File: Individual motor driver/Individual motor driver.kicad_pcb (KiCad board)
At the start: 2 copper layers, 92.7 x 95.2 mm, 35 parts, among them P1 CONN_01X02, P2 CONN_01X02, P3 CONN_01X02, P4 CONN_01X02, P5 CONN_01X02, P6 CONN_01X02, P7 CONN_01X04, P8 CONN_01X02, Q1 PN2222A, Q2 PN2222A, Q3 PN2222A, Q4 PN2222A, U1 BluePill_STM32F103C, U2 BluePill_STM32F103C, U3 ACS711xLCTR-12AB, U4 ACS711xLCTR-12AB

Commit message: Update files
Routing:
- net Stall_2: track 0.00 -> 97.5 mm, vias 0 -> 1
- net GND: track 33.0 -> 43.4 mm, vias 0 -> 73
- net 3.3v: track 225.4 -> 221.5 mm, vias 7 -> 6
- net (no net): vias 2 -> 0
- added copper zone on B.Cu, net GND
- added copper zone on F.Cu, net GND

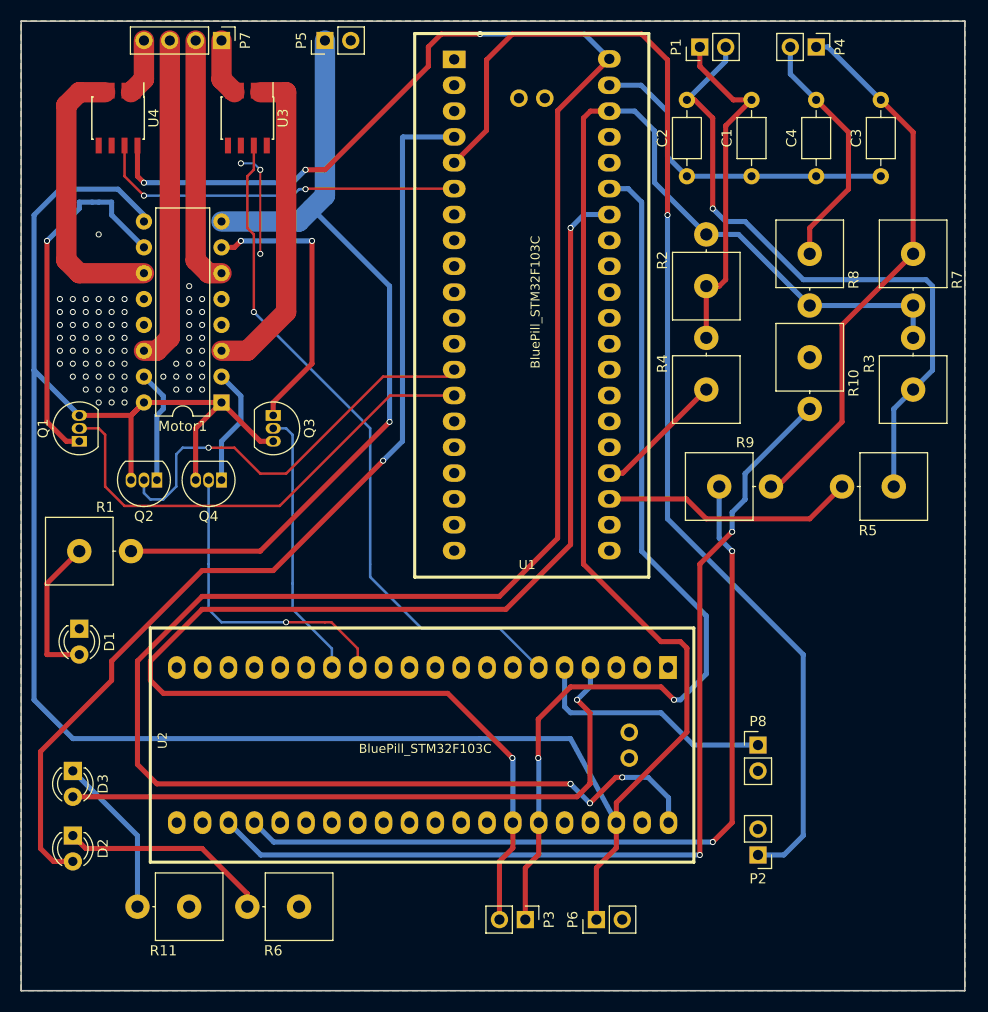
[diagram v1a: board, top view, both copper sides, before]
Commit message: Finished routing and improved some design flaws
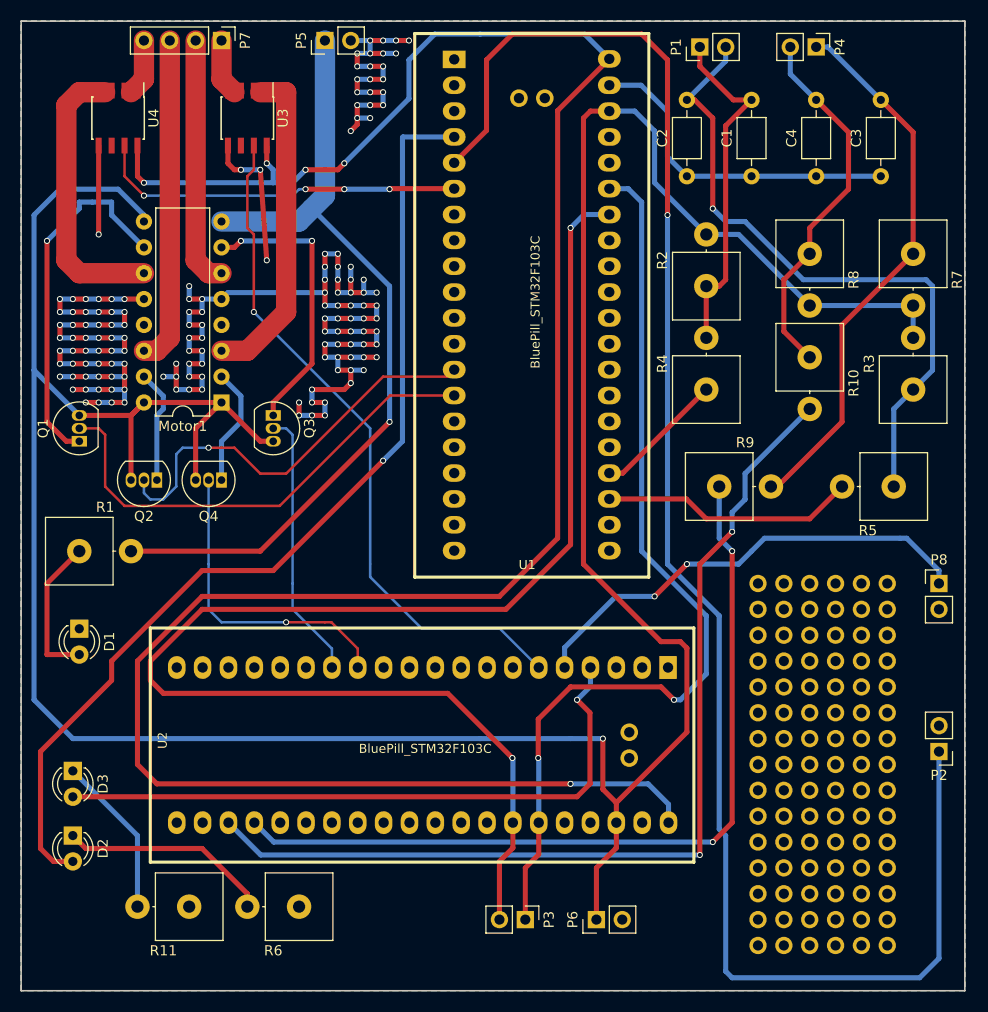
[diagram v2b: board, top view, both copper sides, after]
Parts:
- added REF**: Pin_Header_Straight_1x01_Pitch2.54mm, Pin_Headers:Pin_Header_Straight_1x01_Pitch2.54mm, F.Cu at (130.2, 149.9)
- added REF**: Pin_Header_Straight_1x01_Pitch2.54mm, Pin_Headers:Pin_Header_Straight_1x01_Pitch2.54mm, F.Cu at (122.6, 147.3)
- added REF**: Pin_Header_Straight_1x01_Pitch2.54mm, Pin_Headers:Pin_Header_Straight_1x01_Pitch2.54mm, F.Cu at (120.0, 147.3)
- added REF**: Pin_Header_Straight_1x01_Pitch2.54mm, Pin_Headers:Pin_Header_Straight_1x01_Pitch2.54mm, F.Cu at (117.5, 147.3)
- added REF**: Pin_Header_Straight_1x01_Pitch2.54mm, Pin_Headers:Pin_Header_Straight_1x01_Pitch2.54mm, F.Cu at (130.2, 144.8)
- added REF**: Pin_Header_Straight_1x01_Pitch2.54mm, Pin_Headers:Pin_Header_Straight_1x01_Pitch2.54mm, F.Cu at (127.6, 144.8)
- added REF**: Pin_Header_Straight_1x01_Pitch2.54mm, Pin_Headers:Pin_Header_Straight_1x01_Pitch2.54mm, F.Cu at (125.1, 144.8)
- added REF**: Pin_Header_Straight_1x01_Pitch2.54mm, Pin_Headers:Pin_Header_Straight_1x01_Pitch2.54mm, F.Cu at (122.6, 144.8)
- added REF**: Pin_Header_Straight_1x01_Pitch2.54mm, Pin_Headers:Pin_Header_Straight_1x01_Pitch2.54mm, F.Cu at (120.0, 144.8)
- added REF**: Pin_Header_Straight_1x01_Pitch2.54mm, Pin_Headers:Pin_Header_Straight_1x01_Pitch2.54mm, F.Cu at (117.5, 144.8)
- added REF**: Pin_Header_Straight_1x01_Pitch2.54mm, Pin_Headers:Pin_Header_Straight_1x01_Pitch2.54mm, F.Cu at (130.2, 142.2)
- added REF**: Pin_Header_Straight_1x01_Pitch2.54mm, Pin_Headers:Pin_Header_Straight_1x01_Pitch2.54mm, F.Cu at (127.6, 149.9)
- added REF**: Pin_Header_Straight_1x01_Pitch2.54mm, Pin_Headers:Pin_Header_Straight_1x01_Pitch2.54mm, F.Cu at (127.6, 142.2)
- added REF**: Pin_Header_Straight_1x01_Pitch2.54mm, Pin_Headers:Pin_Header_Straight_1x01_Pitch2.54mm, F.Cu at (125.1, 142.2)
- added REF**: Pin_Header_Straight_1x01_Pitch2.54mm, Pin_Headers:Pin_Header_Straight_1x01_Pitch2.54mm, F.Cu at (122.6, 142.2)
- added REF**: Pin_Header_Straight_1x01_Pitch2.54mm, Pin_Headers:Pin_Header_Straight_1x01_Pitch2.54mm, F.Cu at (120.0, 142.2)
- added REF**: Pin_Header_Straight_1x01_Pitch2.54mm, Pin_Headers:Pin_Header_Straight_1x01_Pitch2.54mm, F.Cu at (117.5, 142.2)
- added REF**: Pin_Header_Straight_1x01_Pitch2.54mm, Pin_Headers:Pin_Header_Straight_1x01_Pitch2.54mm, F.Cu at (130.2, 139.7)
- added REF**: Pin_Header_Straight_1x01_Pitch2.54mm, Pin_Headers:Pin_Header_Straight_1x01_Pitch2.54mm, F.Cu at (127.6, 139.7)
- added REF**: Pin_Header_Straight_1x01_Pitch2.54mm, Pin_Headers:Pin_Header_Straight_1x01_Pitch2.54mm, F.Cu at (125.1, 139.7)
- added REF**: Pin_Header_Straight_1x01_Pitch2.54mm, Pin_Headers:Pin_Header_Straight_1x01_Pitch2.54mm, F.Cu at (122.6, 139.7)
- added REF**: Pin_Header_Straight_1x01_Pitch2.54mm, Pin_Headers:Pin_Header_Straight_1x01_Pitch2.54mm, F.Cu at (120.0, 139.7)
- added REF**: Pin_Header_Straight_1x01_Pitch2.54mm, Pin_Headers:Pin_Header_Straight_1x01_Pitch2.54mm, F.Cu at (125.1, 149.9)
- added REF**: Pin_Header_Straight_1x01_Pitch2.54mm, Pin_Headers:Pin_Header_Straight_1x01_Pitch2.54mm, F.Cu at (117.5, 139.7)
- added REF**: Pin_Header_Straight_1x01_Pitch2.54mm, Pin_Headers:Pin_Header_Straight_1x01_Pitch2.54mm, F.Cu at (130.2, 137.2)
- added REF**: Pin_Header_Straight_1x01_Pitch2.54mm, Pin_Headers:Pin_Header_Straight_1x01_Pitch2.54mm, F.Cu at (127.6, 137.2)
- added REF**: Pin_Header_Straight_1x01_Pitch2.54mm, Pin_Headers:Pin_Header_Straight_1x01_Pitch2.54mm, F.Cu at (125.1, 137.2)
- added REF**: Pin_Header_Straight_1x01_Pitch2.54mm, Pin_Headers:Pin_Header_Straight_1x01_Pitch2.54mm, F.Cu at (122.6, 137.2)
- added REF**: Pin_Header_Straight_1x01_Pitch2.54mm, Pin_Headers:Pin_Header_Straight_1x01_Pitch2.54mm, F.Cu at (120.0, 137.2)
- added REF**: Pin_Header_Straight_1x01_Pitch2.54mm, Pin_Headers:Pin_Header_Straight_1x01_Pitch2.54mm, F.Cu at (117.5, 137.2)
- added REF**: Pin_Header_Straight_1x01_Pitch2.54mm, Pin_Headers:Pin_Header_Straight_1x01_Pitch2.54mm, F.Cu at (130.2, 134.6)
- added REF**: Pin_Header_Straight_1x01_Pitch2.54mm, Pin_Headers:Pin_Header_Straight_1x01_Pitch2.54mm, F.Cu at (127.6, 134.6)
- added REF**: Pin_Header_Straight_1x01_Pitch2.54mm, Pin_Headers:Pin_Header_Straight_1x01_Pitch2.54mm, F.Cu at (125.1, 134.6)
- added REF**: Pin_Header_Straight_1x01_Pitch2.54mm, Pin_Headers:Pin_Header_Straight_1x01_Pitch2.54mm, F.Cu at (122.6, 149.9)
- added REF**: Pin_Header_Straight_1x01_Pitch2.54mm, Pin_Headers:Pin_Header_Straight_1x01_Pitch2.54mm, F.Cu at (122.6, 134.6)
- added REF**: Pin_Header_Straight_1x01_Pitch2.54mm, Pin_Headers:Pin_Header_Straight_1x01_Pitch2.54mm, F.Cu at (120.0, 134.6)
- added REF**: Pin_Header_Straight_1x01_Pitch2.54mm, Pin_Headers:Pin_Header_Straight_1x01_Pitch2.54mm, F.Cu at (117.5, 134.6)
- added REF**: Pin_Header_Straight_1x01_Pitch2.54mm, Pin_Headers:Pin_Header_Straight_1x01_Pitch2.54mm, F.Cu at (130.2, 132.1)
- added REF**: Pin_Header_Straight_1x01_Pitch2.54mm, Pin_Headers:Pin_Header_Straight_1x01_Pitch2.54mm, F.Cu at (127.6, 132.1)
- added REF**: Pin_Header_Straight_1x01_Pitch2.54mm, Pin_Headers:Pin_Header_Straight_1x01_Pitch2.54mm, F.Cu at (125.1, 132.1)
- added REF**: Pin_Header_Straight_1x01_Pitch2.54mm, Pin_Headers:Pin_Header_Straight_1x01_Pitch2.54mm, F.Cu at (122.6, 132.1)
- added REF**: Pin_Header_Straight_1x01_Pitch2.54mm, Pin_Headers:Pin_Header_Straight_1x01_Pitch2.54mm, F.Cu at (120.0, 132.1)
- added REF**: Pin_Header_Straight_1x01_Pitch2.54mm, Pin_Headers:Pin_Header_Straight_1x01_Pitch2.54mm, F.Cu at (117.5, 132.1)
- added REF**: Pin_Header_Straight_1x01_Pitch2.54mm, Pin_Headers:Pin_Header_Straight_1x01_Pitch2.54mm, F.Cu at (130.2, 129.5)
- added REF**: Pin_Header_Straight_1x01_Pitch2.54mm, Pin_Headers:Pin_Header_Straight_1x01_Pitch2.54mm, F.Cu at (120.0, 149.9)
- added REF**: Pin_Header_Straight_1x01_Pitch2.54mm, Pin_Headers:Pin_Header_Straight_1x01_Pitch2.54mm, F.Cu at (127.6, 129.5)
- added REF**: Pin_Header_Straight_1x01_Pitch2.54mm, Pin_Headers:Pin_Header_Straight_1x01_Pitch2.54mm, F.Cu at (125.1, 129.5)
- added REF**: Pin_Header_Straight_1x01_Pitch2.54mm, Pin_Headers:Pin_Header_Straight_1x01_Pitch2.54mm, F.Cu at (122.6, 129.5)
- added REF**: Pin_Header_Straight_1x01_Pitch2.54mm, Pin_Headers:Pin_Header_Straight_1x01_Pitch2.54mm, F.Cu at (120.0, 129.5)
- added REF**: Pin_Header_Straight_1x01_Pitch2.54mm, Pin_Headers:Pin_Header_Straight_1x01_Pitch2.54mm, F.Cu at (117.5, 129.5)
- added REF**: Pin_Header_Straight_1x01_Pitch2.54mm, Pin_Headers:Pin_Header_Straight_1x01_Pitch2.54mm, F.Cu at (130.2, 127.0)
- added REF**: Pin_Header_Straight_1x01_Pitch2.54mm, Pin_Headers:Pin_Header_Straight_1x01_Pitch2.54mm, F.Cu at (127.6, 127.0)
- added REF**: Pin_Header_Straight_1x01_Pitch2.54mm, Pin_Headers:Pin_Header_Straight_1x01_Pitch2.54mm, F.Cu at (125.1, 127.0)
- added REF**: Pin_Header_Straight_1x01_Pitch2.54mm, Pin_Headers:Pin_Header_Straight_1x01_Pitch2.54mm, F.Cu at (122.6, 127.0)
- added REF**: Pin_Header_Straight_1x01_Pitch2.54mm, Pin_Headers:Pin_Header_Straight_1x01_Pitch2.54mm, F.Cu at (120.0, 127.0)
- added REF**: Pin_Header_Straight_1x01_Pitch2.54mm, Pin_Headers:Pin_Header_Straight_1x01_Pitch2.54mm, F.Cu at (117.5, 149.9)
- added REF**: Pin_Header_Straight_1x01_Pitch2.54mm, Pin_Headers:Pin_Header_Straight_1x01_Pitch2.54mm, F.Cu at (117.5, 127.0)
- added REF**: Pin_Header_Straight_1x01_Pitch2.54mm, Pin_Headers:Pin_Header_Straight_1x01_Pitch2.54mm, F.Cu at (130.2, 124.5)
- added REF**: Pin_Header_Straight_1x01_Pitch2.54mm, Pin_Headers:Pin_Header_Straight_1x01_Pitch2.54mm, F.Cu at (127.6, 124.5)
- added REF**: Pin_Header_Straight_1x01_Pitch2.54mm, Pin_Headers:Pin_Header_Straight_1x01_Pitch2.54mm, F.Cu at (125.1, 124.5)
- added REF**: Pin_Header_Straight_1x01_Pitch2.54mm, Pin_Headers:Pin_Header_Straight_1x01_Pitch2.54mm, F.Cu at (122.6, 124.5)
- added REF**: Pin_Header_Straight_1x01_Pitch2.54mm, Pin_Headers:Pin_Header_Straight_1x01_Pitch2.54mm, F.Cu at (120.0, 124.5)
- added REF**: Pin_Header_Straight_1x01_Pitch2.54mm, Pin_Headers:Pin_Header_Straight_1x01_Pitch2.54mm, F.Cu at (117.5, 124.5)
- added REF**: Pin_Header_Straight_1x01_Pitch2.54mm, Pin_Headers:Pin_Header_Straight_1x01_Pitch2.54mm, F.Cu at (130.2, 121.9)
- added REF**: Pin_Header_Straight_1x01_Pitch2.54mm, Pin_Headers:Pin_Header_Straight_1x01_Pitch2.54mm, F.Cu at (127.6, 121.9)
- added REF**: Pin_Header_Straight_1x01_Pitch2.54mm, Pin_Headers:Pin_Header_Straight_1x01_Pitch2.54mm, F.Cu at (125.1, 121.9)
- added REF**: Pin_Header_Straight_1x01_Pitch2.54mm, Pin_Headers:Pin_Header_Straight_1x01_Pitch2.54mm, F.Cu at (130.2, 147.3)
- added REF**: Pin_Header_Straight_1x01_Pitch2.54mm, Pin_Headers:Pin_Header_Straight_1x01_Pitch2.54mm, F.Cu at (122.6, 121.9)
- added REF**: Pin_Header_Straight_1x01_Pitch2.54mm, Pin_Headers:Pin_Header_Straight_1x01_Pitch2.54mm, F.Cu at (120.0, 121.9)
- added REF**: Pin_Header_Straight_1x01_Pitch2.54mm, Pin_Headers:Pin_Header_Straight_1x01_Pitch2.54mm, F.Cu at (117.5, 121.9)
- added REF**: Pin_Header_Straight_1x01_Pitch2.54mm, Pin_Headers:Pin_Header_Straight_1x01_Pitch2.54mm, F.Cu at (130.2, 119.4)
- added REF**: Pin_Header_Straight_1x01_Pitch2.54mm, Pin_Headers:Pin_Header_Straight_1x01_Pitch2.54mm, F.Cu at (127.6, 119.4)
- added REF**: Pin_Header_Straight_1x01_Pitch2.54mm, Pin_Headers:Pin_Header_Straight_1x01_Pitch2.54mm, F.Cu at (125.1, 119.4)
- added REF**: Pin_Header_Straight_1x01_Pitch2.54mm, Pin_Headers:Pin_Header_Straight_1x01_Pitch2.54mm, F.Cu at (122.6, 119.4)
- added REF**: Pin_Header_Straight_1x01_Pitch2.54mm, Pin_Headers:Pin_Header_Straight_1x01_Pitch2.54mm, F.Cu at (120.0, 119.4)
- added REF**: Pin_Header_Straight_1x01_Pitch2.54mm, Pin_Headers:Pin_Header_Straight_1x01_Pitch2.54mm, F.Cu at (117.5, 119.4)
- added REF**: Pin_Header_Straight_1x01_Pitch2.54mm, Pin_Headers:Pin_Header_Straight_1x01_Pitch2.54mm, F.Cu at (130.2, 116.8)
- added REF**: Pin_Header_Straight_1x01_Pitch2.54mm, Pin_Headers:Pin_Header_Straight_1x01_Pitch2.54mm, F.Cu at (127.6, 147.3)
- added REF**: Pin_Header_Straight_1x01_Pitch2.54mm, Pin_Headers:Pin_Header_Straight_1x01_Pitch2.54mm, F.Cu at (127.6, 116.8)
- added REF**: Pin_Header_Straight_1x01_Pitch2.54mm, Pin_Headers:Pin_Header_Straight_1x01_Pitch2.54mm, F.Cu at (125.1, 116.8)
- added REF**: Pin_Header_Straight_1x01_Pitch2.54mm, Pin_Headers:Pin_Header_Straight_1x01_Pitch2.54mm, F.Cu at (122.6, 116.8)
- added REF**: Pin_Header_Straight_1x01_Pitch2.54mm, Pin_Headers:Pin_Header_Straight_1x01_Pitch2.54mm, F.Cu at (120.0, 116.8)
- added REF**: Pin_Header_Straight_1x01_Pitch2.54mm, Pin_Headers:Pin_Header_Straight_1x01_Pitch2.54mm, F.Cu at (117.5, 116.8)
- added REF**: Pin_Header_Straight_1x01_Pitch2.54mm, Pin_Headers:Pin_Header_Straight_1x01_Pitch2.54mm, F.Cu at (130.2, 114.3)
- added REF**: Pin_Header_Straight_1x01_Pitch2.54mm, Pin_Headers:Pin_Header_Straight_1x01_Pitch2.54mm, F.Cu at (127.6, 114.3)
- added REF**: Pin_Header_Straight_1x01_Pitch2.54mm, Pin_Headers:Pin_Header_Straight_1x01_Pitch2.54mm, F.Cu at (125.1, 114.3)
- added REF**: Pin_Header_Straight_1x01_Pitch2.54mm, Pin_Headers:Pin_Header_Straight_1x01_Pitch2.54mm, F.Cu at (122.6, 114.3)
- added REF**: Pin_Header_Straight_1x01_Pitch2.54mm, Pin_Headers:Pin_Header_Straight_1x01_Pitch2.54mm, F.Cu at (120.0, 114.3)
- added REF**: Pin_Header_Straight_1x01_Pitch2.54mm, Pin_Headers:Pin_Header_Straight_1x01_Pitch2.54mm, F.Cu at (125.1, 147.3)
- added REF**: Pin_Header_Straight_1x01_Pitch2.54mm, Pin_Headers:Pin_Header_Straight_1x01_Pitch2.54mm, F.Cu at (117.5, 114.3)
- moved P8 23.8 mm to (135.3, 114.3)
- moved P2 20.5 mm to (135.3, 130.8)
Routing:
- net GND: track 43.4 -> 254.1 mm, vias 73 -> 149
- net Limit2: track 118.3 -> 165.5 mm
- net Limit1: track 24.4 -> 45.8 mm, vias 0 -> 2
- net Net-(C4-Pad2): track 24.3 -> 36.5 mm
- net 3.3v: track 221.5 -> 224.1 mm, vias 6 -> 5
- net 5V: track 303.6 -> 304.2 mm, vias 0 -> 1
- net M2:Current: vias 2 -> 4

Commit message: PCB updates
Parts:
- added P9: CONN_01X02, Connector_PinHeader_2.54mm:PinHeader_1x02_P2.54mm_Vertical, F.Cu at (94.6, 151.8)
- added REF**: MountingHole_3.2mm_M3, MountingHole:MountingHole_3.2mm_M3, F.Cu at (48.9, 150.5)
- added REF**: MountingHole_3.2mm_M3, MountingHole:MountingHole_3.2mm_M3, F.Cu at (48.9, 62.9)
- added REF**: MountingHole_3.2mm_M3, MountingHole:MountingHole_3.2mm_M3, F.Cu at (134.0, 62.9)
- added REF**: MountingHole_3.2mm_M3, MountingHole:MountingHole_3.2mm_M3, F.Cu at (110.5, 150.5)
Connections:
- REF** pad 1: (no net) -> GND (x6)
- REF** pad 1: (no net) -> 5V (x6)
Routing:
- net 5V: track 304.2 -> 335.6 mm, vias 1 -> 2
- net SDA: track 92.4 -> 96.8 mm
- net SCL: track 138.5 -> 143.0 mm
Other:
- outline, holes or cut-outs redrawn
- board text added: "5V"
- board text added: "Designed and made by Ethan. Class of 2020 https://github.com/ethanleep/robotic-arm"
- board text added: "GND"
- board text added: "Voltage range: 4.5V - 36V Max current: 1A per motor Overall max current: 2A"

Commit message: Misc. Changes to PCB
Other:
- board text added: "Prototyping Area"
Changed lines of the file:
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@@
     (area 45.009999 58.979999 137.870001 154.380001)
     (thickness 1.6)
-    (drawings 45)
+    (drawings 46)
     (tracks 691)
     (zones 0)
@@
   )
   (setup
-    (last_trace_width 0.5)
+    (last_trace_width 0.25)
     (user_trace_width 0.2)
     (user_trace_width 0.25)
@@
     (pad 1 np_thru_hole circle (at 0 0) (size 3.2 3.2) (drill 3.2) (layers *.Cu *.Mask))
   )
+  (gr_text "Prototyping Area" (at 114.3 128.27 90) (layer F.SilkS)
+    (effects (font (size 1.5 1.5) (thickness 0.3)))
+  )
+  (dimension 95.25 (width 0.3) (layer Cmts.User)
+    (gr_text "95.250 mm" (at 25.955001 106.68 270) (layer Cmts.User)
+      (effects (font (size 1.5 1.5) (thickness 0.3)))
+    )
+    (feature1 (pts (xy 49.53 154.305) (xy 24.605001 154.305)))
+    (feature2 (pts (xy 49.53 59.055) (xy 24.605001 59.055)))
+    (crossbar (pts (xy 27.305001 59.055) (xy 27.305001 154.305)))
+    (arrow1a (pts (xy 27.305001 154.305) (xy 26.71858 153.178496)))
+    (arrow1b (pts (xy 27.305001 154.305) (xy 27.891422 153.178496)))
+    (arrow2a (pts (xy 27.305001 59.055) (xy 26.71858 60.181504)))
+    (arrow2b (pts (xy 27.305001 59.055) (xy 27.891422 60.181504)))
+  )
+  (dimension 92.71 (width 0.3) (layer Cmts.User)
+    (gr_text "92.710 mm" (at 91.44 46.275) (layer Cmts.User)
+      (effects (font (size 1.5 1.5) (thickness 0.3)))
+    )
+    (feature1 (pts (xy 137.795 63.5) (xy 137.795 44.925)))
+    (feature2 (pts (xy 45.085 63.5) (xy 45.085 44.925)))
+    (crossbar (pts (xy 45.085 47.625) (xy 137.795 47.625)))
+    (arrow1a (pts (xy 137.795 47.625) (xy 136.668496 48.211421)))
+    (arrow1b (pts (xy 137.795 47.625) (xy 136.668496 47.038579)))
+    (arrow2a (pts (xy 45.085 47.625) (xy 46.211504 48.211421)))
+    (arrow2b (pts (xy 45.085 47.625) (xy 46.211504 47.038579)))
+  )
   (gr_text "Voltage range: 4.5V - 36V\nMax current: 1A per motor\nOverall max current: 2A" (at 60.96 71.12) (layer B.SilkS)
     (effects (font (size 1.5 1.5) (thickness 0.3)) (justify mirror))
@@
     (effects (font (size 1.5 1.5) (thickness 0.3)))
   )
-  (dimension 87.63 (width 0.3) (layer Cmts.User)
-    (gr_text "87.630 mm" (at 88.9 39.29) (layer Cmts.User)
-      (effects (font (size 1.5 1.5) (thickness 0.3)))
-    )
-    (feature1 (pts (xy 132.715 59.055) (xy 132.715 37.94)))
-    (feature2 (pts (xy 45.085 59.055) (xy 45.085 37.94)))
-    (crossbar (pts (xy 45.085 40.64) (xy 132.715 40.64)))
-    (arrow1a (pts (xy 132.715 40.64) (xy 131.588496 41.226421)))
-    (arrow1b (pts (xy 132.715 40.64) (xy 131.588496 40.053579)))
-    (arrow2a (pts (xy 45.085 40.64) (xy 46.211504 41.226421)))
-    (arrow2b (pts (xy 45.085 40.64) (xy 46.211504 40.053579)))
-  )
-  (dimension 97.155 (width 0.3) (layer Cmts.User)
-    (gr_text "97.155 mm" (at 36.115001 107.6325 270) (layer Cmts.User)
-      (effects (font (size 1.5 1.5) (thickness 0.3)))
-    )
-    (feature1 (pts (xy 45.085 156.21) (xy 34.765001 156.21)))
-    (feature2 (pts (xy 45.085 59.055) (xy 34.765001 59.055)))
-    (crossbar (pts (xy 37.465001 59.055) (xy 37.465001 156.21)))
-    (arrow1a (pts (xy 37.465001 156.21) (xy 36.87858 155.083496)))
-    (arrow1b (pts (xy 37.465001 156.21) (xy 38.051422 155.083496)))
-    (arrow2a (pts (xy 37.465001 59.055) (xy 36.87858 60.181504)))
-    (arrow2b (pts (xy 37.465001 59.055) (xy 38.051422 60.181504)))
-  )
   (segment (start 52.705 71.28) (end 52.705 80.01) (width 0.5) (layer F.Cu) (net 1))

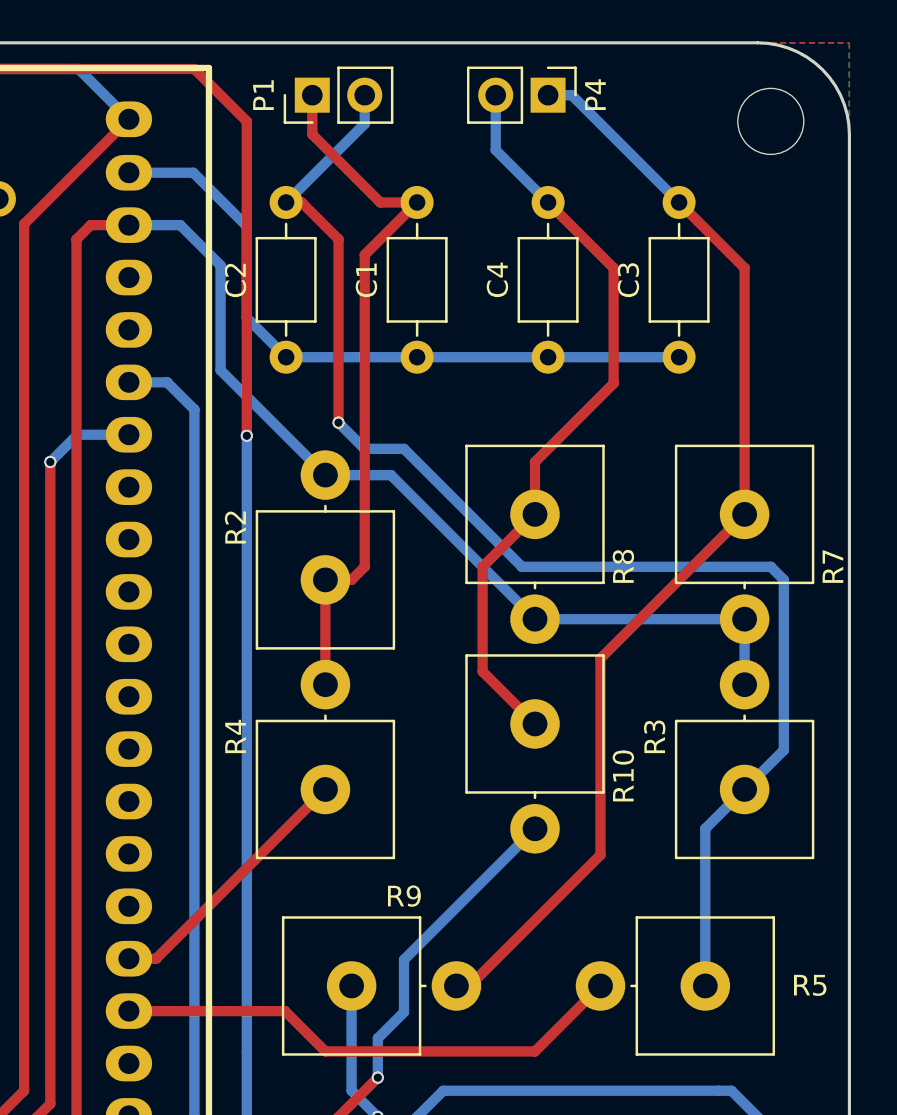
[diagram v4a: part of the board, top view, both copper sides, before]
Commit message: Fixed rotary encoder filter
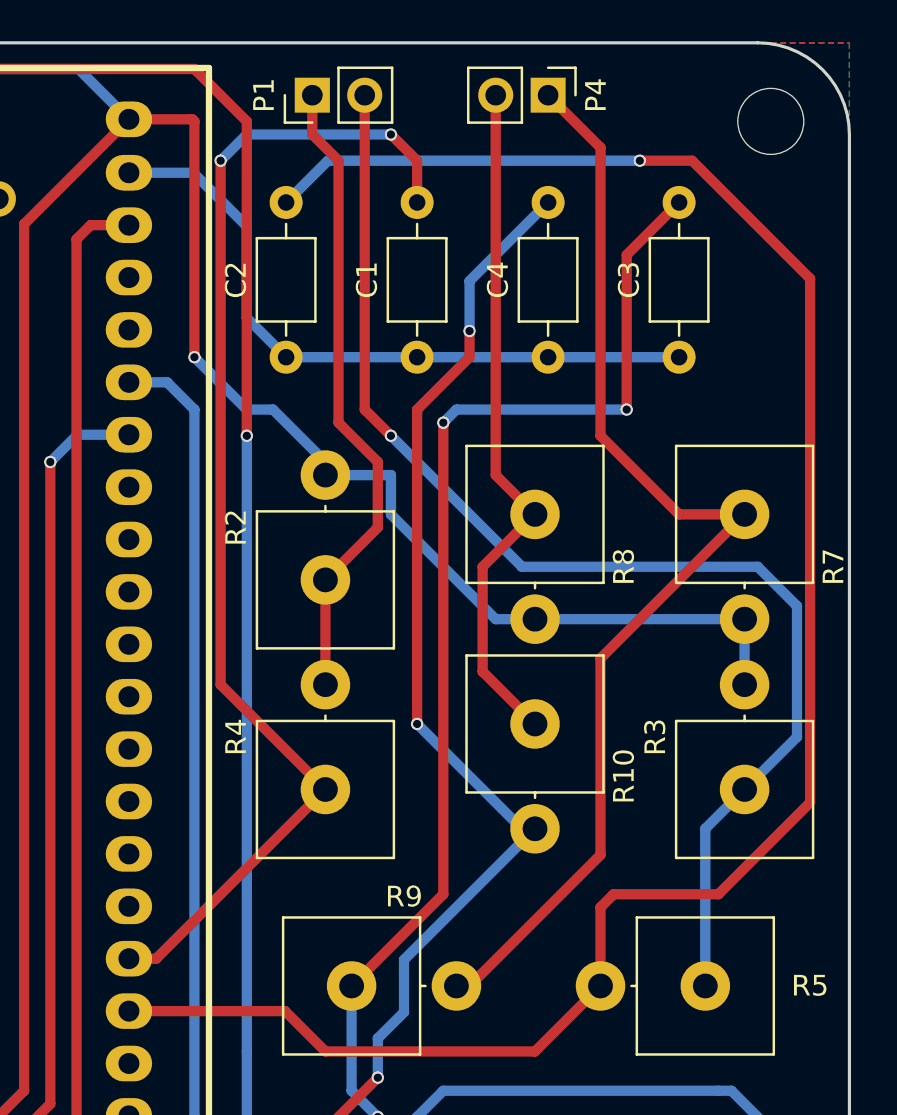
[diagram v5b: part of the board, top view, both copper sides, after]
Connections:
- C1 pad 2: Net-(C1-Pad2) -> Rotary_Encoder_2B
- C2 pad 2: Net-(C2-Pad2) -> Rotary_Encoder_2A
- C3 pad 2: Net-(C3-Pad2) -> Rotary_Encoder_1B
- C4 pad 2: Net-(C4-Pad2) -> Rotary_Encoder_1A
- P1 pad 1: Net-(C1-Pad2) -> Net-(P1-Pad1)
- P1 pad 2: Net-(C2-Pad2) -> Net-(P1-Pad2)
- P4 pad 1: Net-(C3-Pad2) -> Net-(P4-Pad1)
- P4 pad 2: Net-(C4-Pad2) -> Net-(P4-Pad2)
- R10 pad 1: Net-(C4-Pad2) -> Net-(P4-Pad2)
- R2 pad 1: Net-(C1-Pad2) -> Net-(P1-Pad1)
- R2 pad 2: 5V -> 3.3v
- R3 pad 1: Net-(C2-Pad2) -> Net-(P1-Pad2)
- R3 pad 2: 5V -> 3.3v
- R4 pad 2: Net-(C1-Pad2) -> Net-(P1-Pad1)
- R5 pad 1: Net-(C2-Pad2) -> Net-(P1-Pad2)
- R7 pad 1: Net-(C3-Pad2) -> Net-(P4-Pad1)
- R7 pad 2: 5V -> 3.3v
- R8 pad 1: Net-(C4-Pad2) -> Net-(P4-Pad2)
- R8 pad 2: 5V -> 3.3v
- R9 pad 2: Net-(C3-Pad2) -> Net-(P4-Pad1)
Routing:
- net Rotary_Encoder_2A: track 25.0 -> 95.1 mm, vias 0 -> 1
- net Net-(C2-Pad2): track 65.0 -> 0.00 mm, vias 1 -> 0
- net Net-(P1-Pad2): track 0.00 -> 60.4 mm, vias 0 -> 1
- net Net-(P4-Pad1): track 0.00 -> 55.1 mm
- net Net-(C3-Pad2): track 54.0 -> 0.00 mm
- net 3.3v: track 224.1 -> 275.3 mm, vias 5 -> 6
- net Rotary_Encoder_1B: track 82.1 -> 131.5 mm, vias 2 -> 4
- net Rotary_Encoder_2B: track 12.9 -> 58.1 mm, vias 0 -> 2
- net 5V: track 335.6 -> 291.7 mm
- net Net-(C4-Pad2): track 36.5 -> 0.00 mm
- net Rotary_Encoder_1A: track 95.9 -> 131.6 mm, vias 2 -> 4
- net Net-(C1-Pad2): track 34.4 -> 0.00 mm
- net Net-(P4-Pad2): track 0.00 -> 33.4 mm
- net Net-(P1-Pad1): track 0.00 -> 31.1 mm
